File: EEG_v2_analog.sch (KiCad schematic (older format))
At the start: 50 parts, among them U1 ADS1299IPAGR

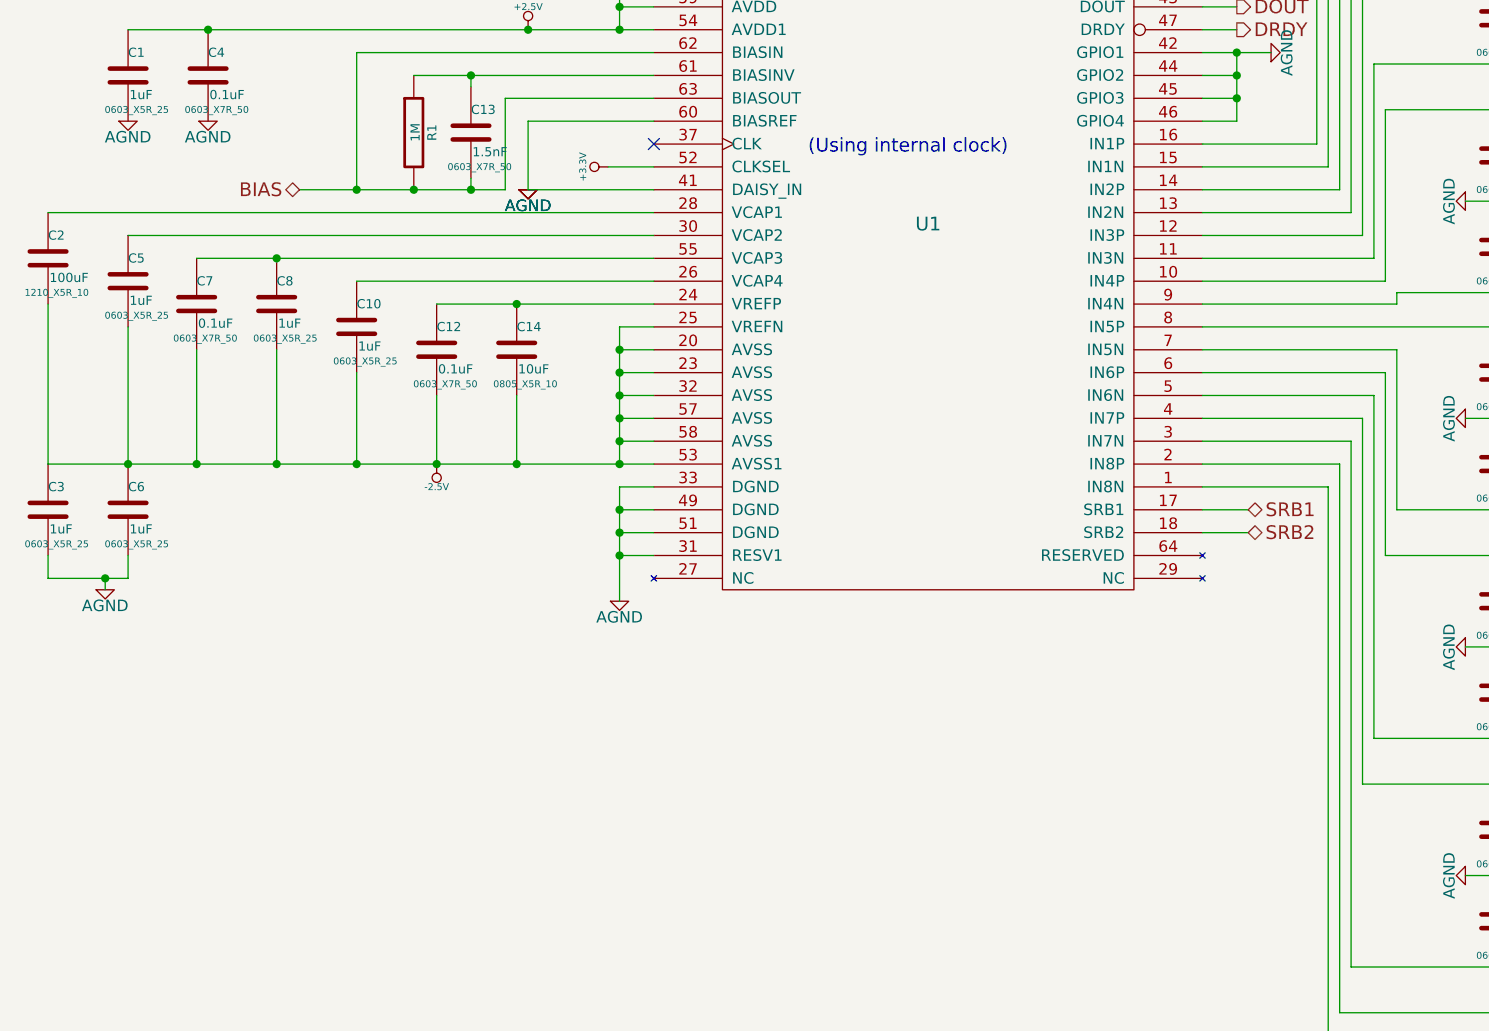
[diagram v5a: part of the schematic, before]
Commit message: Add RC to SRB1
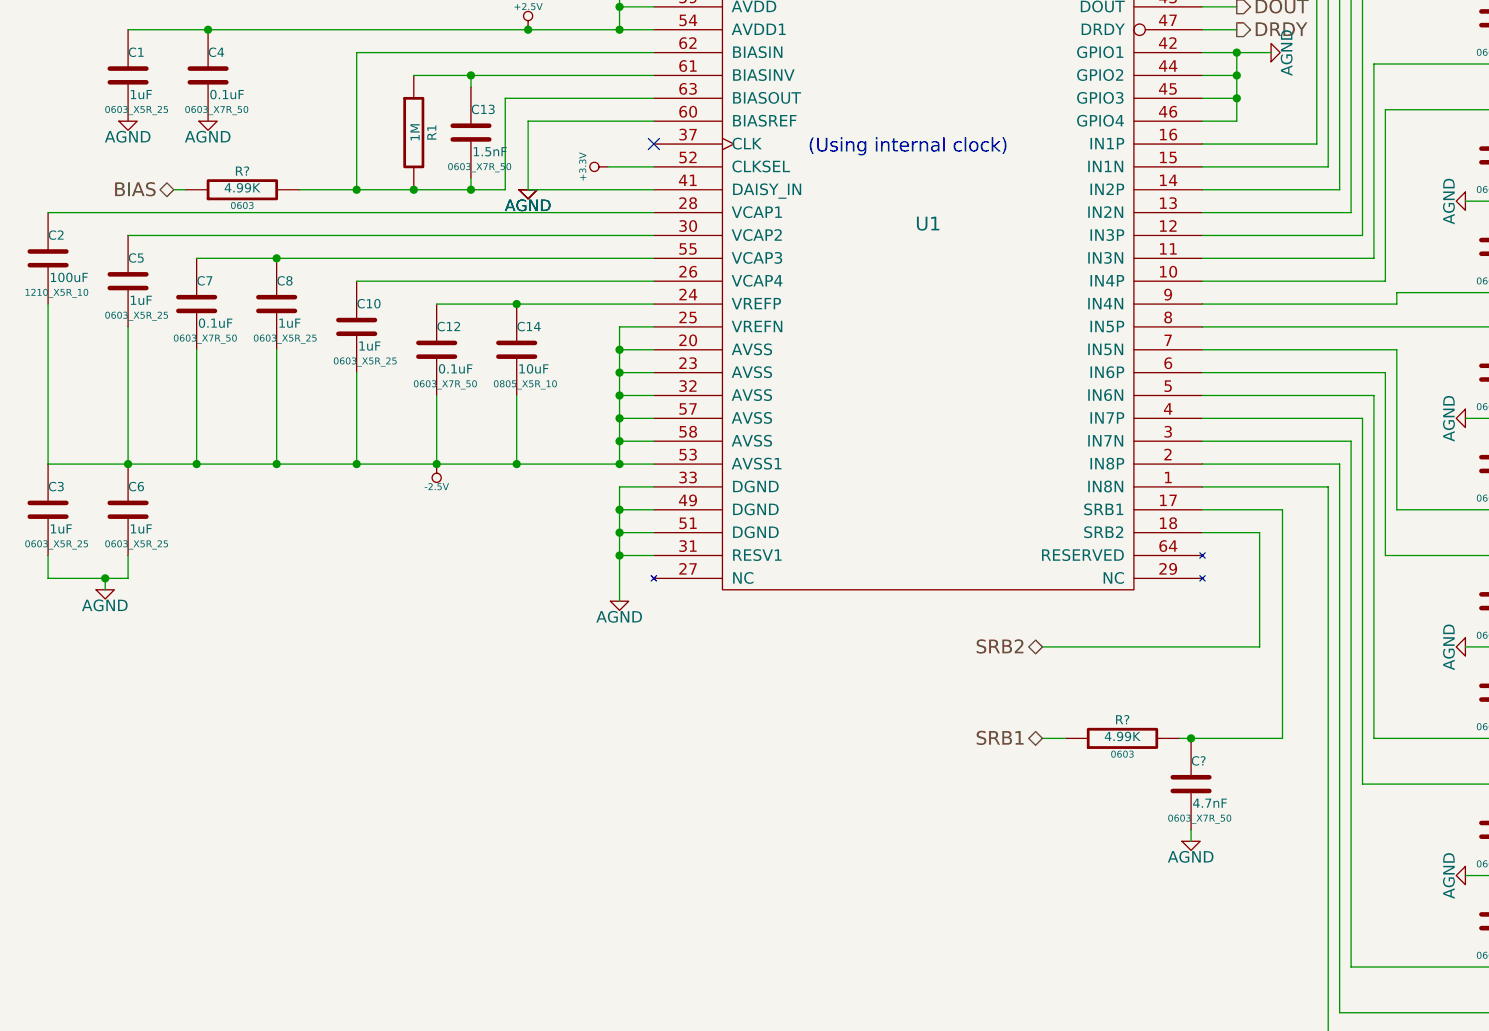
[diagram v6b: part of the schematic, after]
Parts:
- added C?: 4.7nF, 0603_X7R_50, symbol C
- added R? (x2): 4.99K, 0603, symbol R
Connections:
- net AGND: now also C?.2
- net BIAS: now also R?.1; no longer C13.2, R1.2, U1.62 (BIASIN), U1.63 (BIASOUT)
- net SRB1: now also R?.1; no longer U1.17 (SRB1)
- new net: C?.1, R?.2, U1.17 (SRB1)
- new net: C13.2, R1.2, R?.2, U1.62 (BIASIN), U1.63 (BIASOUT)
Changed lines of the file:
@@
 Wire Wire Line
 	6300 5350 5700 5350
-Text HLabel 5900 5550 2    60   BiDi ~ 0
+Text HLabel 5000 6550 0    60   BiDi ~ 0
 SRB1
-Text HLabel 5900 5650 2    60   BiDi ~ 0
+Text HLabel 5000 6150 0    60   BiDi ~ 0
 SRB2
 Wire Wire Line
-	5700 5550 5900 5550
+	5700 5550 6050 5550
 Wire Wire Line
-	5900 5650 5700 5650
-Text HLabel 1750 4150 0    60   BiDi ~ 0
+	5700 5650 5950 5650
+Text HLabel 1200 4150 0    60   BiDi ~ 0
 BIAS
+$Comp
+L R R?
+U 1 1 54C81B51
+P 1500 4150
+F 0 "R?" V 1580 4150 40  0000 C CNN
+F 1 "4.99K" V 1507 4151 40  0000 C CNN
+F 2 "0603" V 1430 4150 30  0000 C CNN
+F 3 "~" H 1500 4150 30  0000 C CNN
+	1    1500 4150
+	0    -1   -1   0
+$EndComp
+Wire Wire Line
+	1200 4150 1250 4150
+$Comp
+L C C?
+U 1 1 54C81E5C
+P 5650 6750
+F 0 "C?" H 5650 6850 40  0000 L CNN
+F 1 "4.7nF" H 5656 6665 40  0000 L CNN
+F 2 "0603_X7R_50" H 5688 6600 30  0000 C CNN
+F 3 "~" H 5650 6750 60  0000 C CNN
+	1    5650 6750
+	1    0    0    -1
+$EndComp
+$Comp
+L R R?
+U 1 1 54C81E67
+P 5350 6550
+F 0 "R?" V 5430 6550 40  0000 C CNN
+F 1 "4.99K" V 5357 6551 40  0000 C CNN
+F 2 "0603" V 5280 6550 30  0000 C CNN
+F 3 "~" H 5350 6550 30  0000 C CNN
+	1    5350 6550
+	0    -1   -1   0
+$EndComp
+Connection ~ 5650 6550
+Wire Wire Line
+	5600 6550 6050 6550
+Wire Wire Line
+	5950 5650 5950 6150
+Wire Wire Line
+	5950 6150 5000 6150
+Wire Wire Line
+	6050 6550 6050 5550
+$Comp
+L AGND #PWR?
+U 1 1 54C824DA
+P 5650 7000
+F 0 "#PWR?" H 5650 7000 40  0001 C CNN
+F 1 "AGND" H 5650 6930 50  0000 C CNN
+F 2 "" H 5650 7000 60  0000 C CNN
+F 3 "" H 5650 7000 60  0000 C CNN
+	1    5650 7000
+	1    0    0    -1
+$EndComp
+Wire Wire Line
+	5650 6950 5650 7000
+Wire Wire Line
+	5100 6550 5000 6550
 $EndSCHEMATC

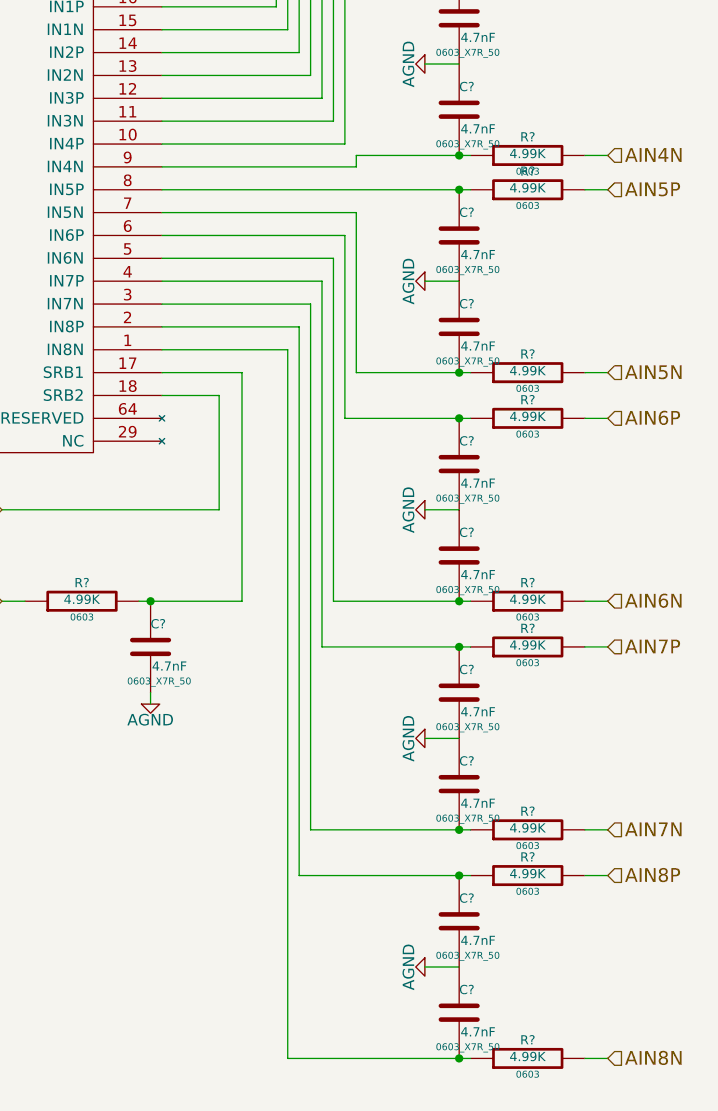
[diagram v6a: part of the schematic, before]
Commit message: Imported sheet pins to main sheet
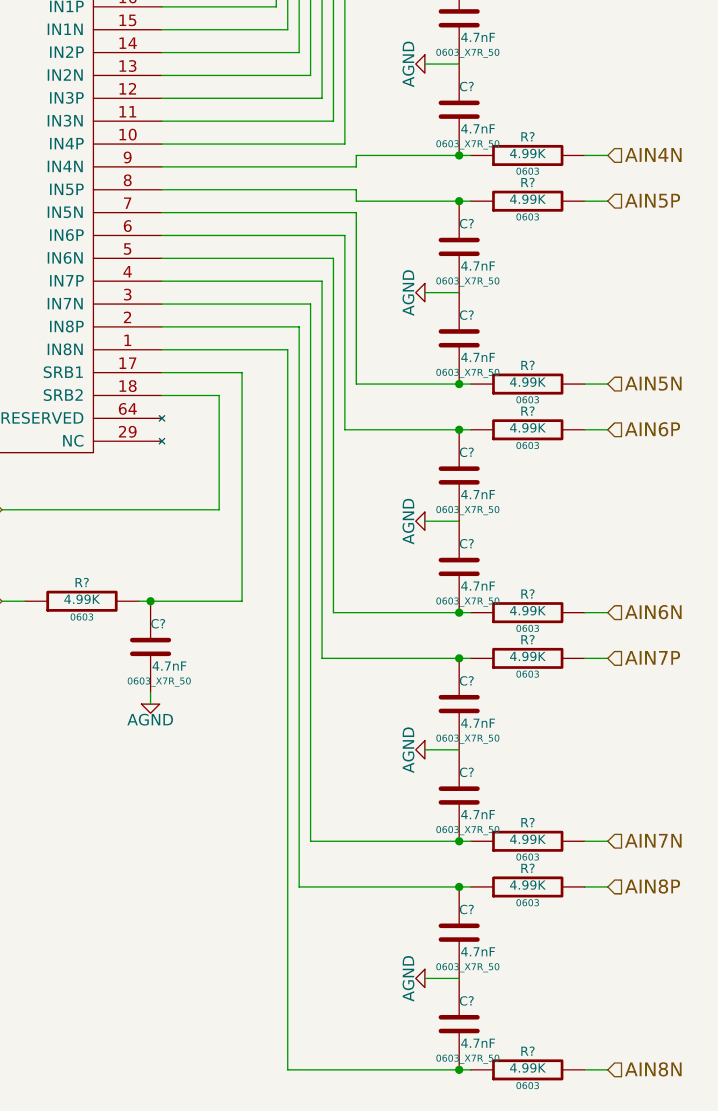
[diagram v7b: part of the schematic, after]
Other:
- moved on the sheet: C?, R?

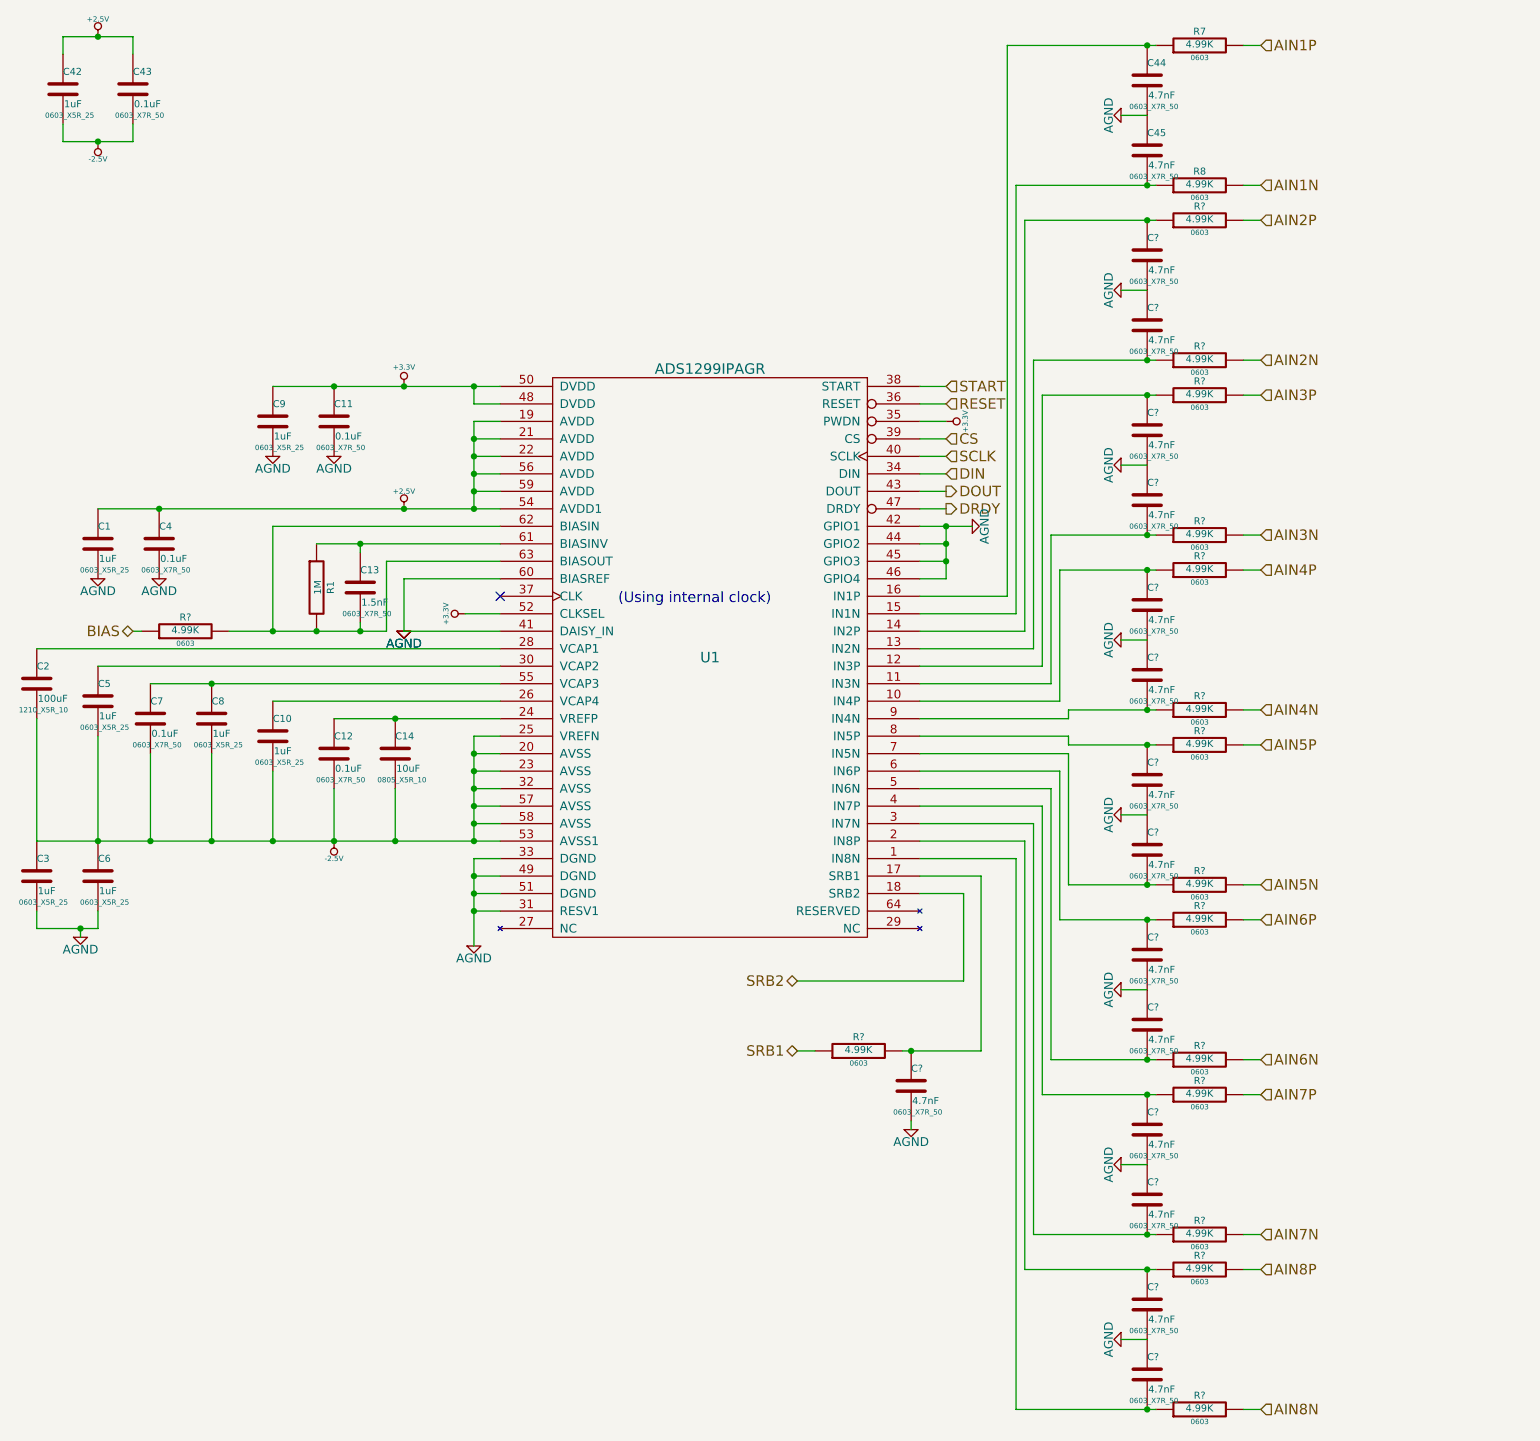
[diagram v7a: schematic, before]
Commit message: Modify libraries to be correct. Add pushbuttons and LEDs. Change switch to toggle.
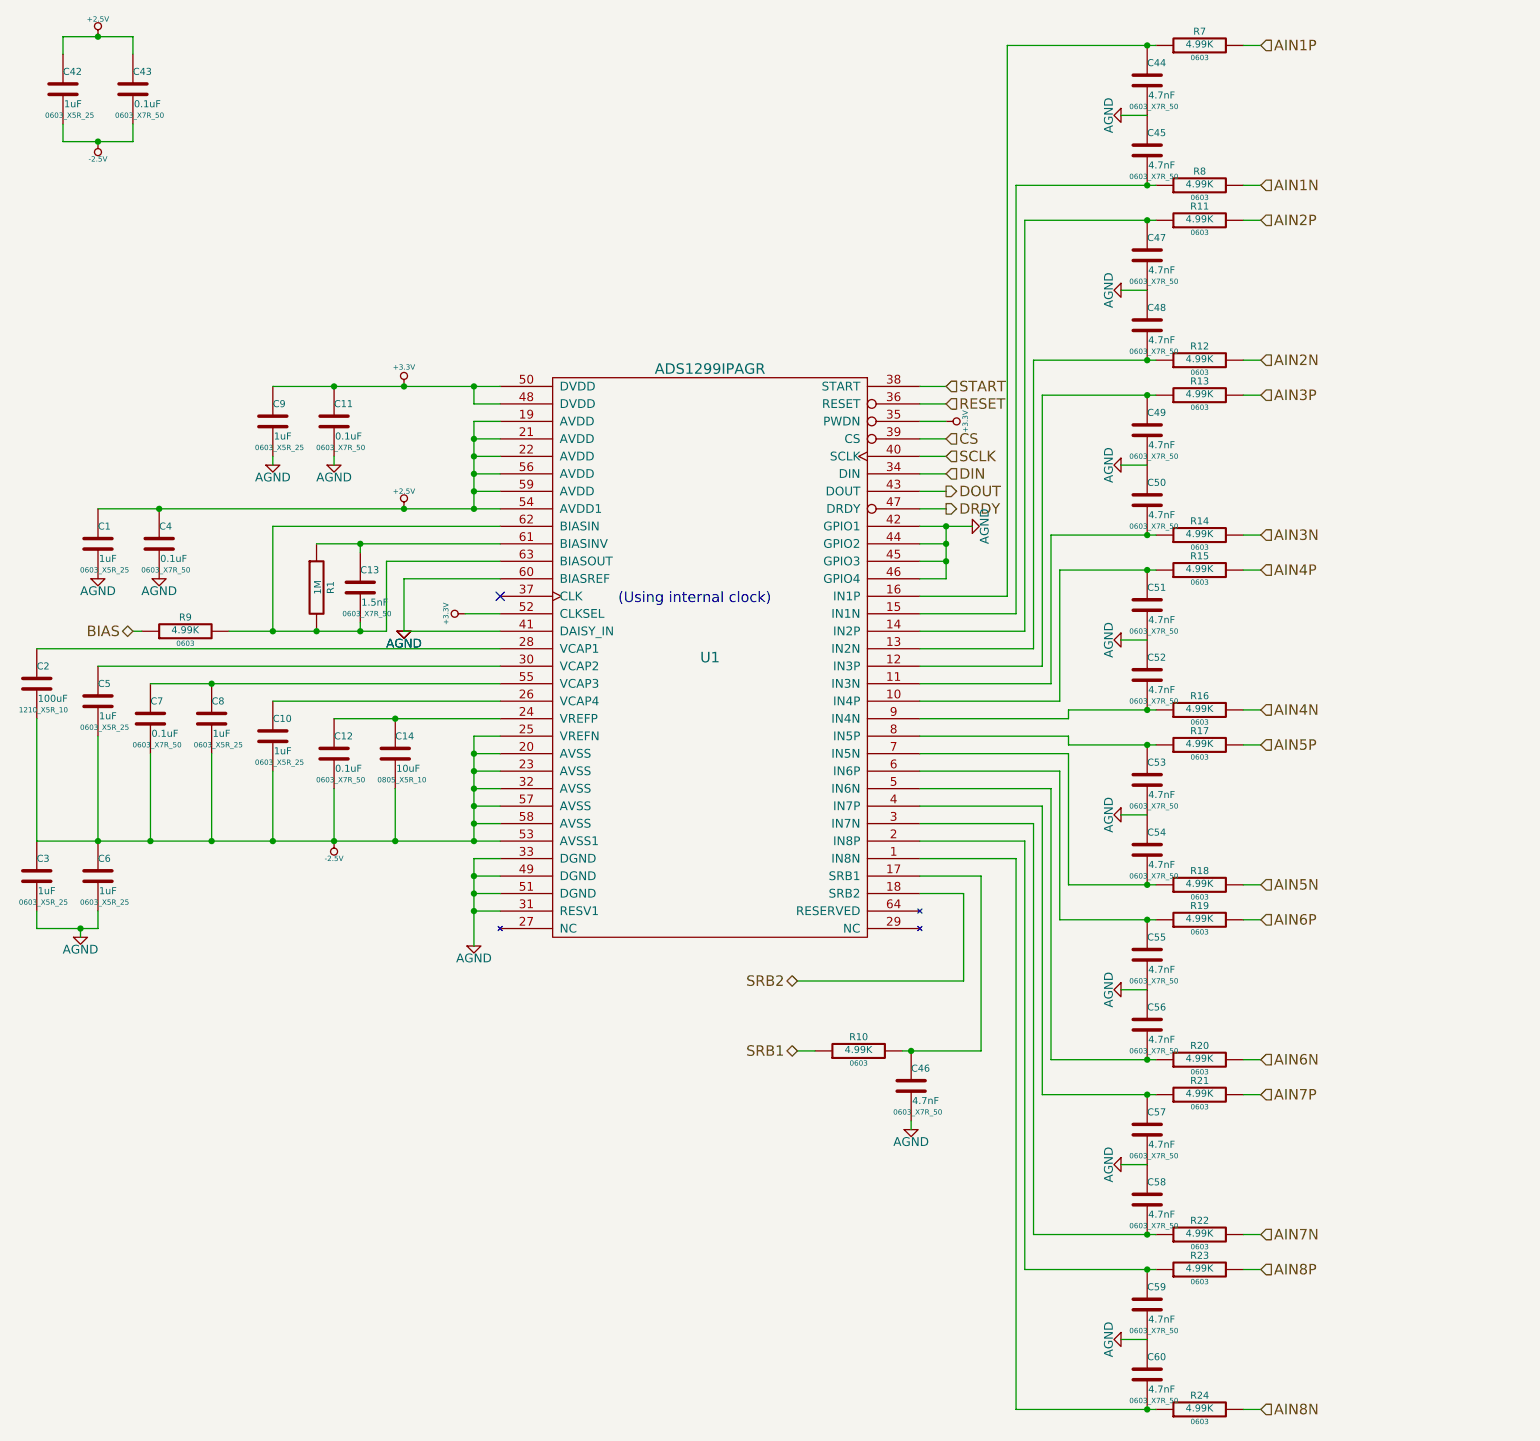
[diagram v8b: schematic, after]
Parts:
- gave numbers to parts that had none: 31
